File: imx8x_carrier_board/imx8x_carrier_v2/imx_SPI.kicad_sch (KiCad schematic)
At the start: 0 parts

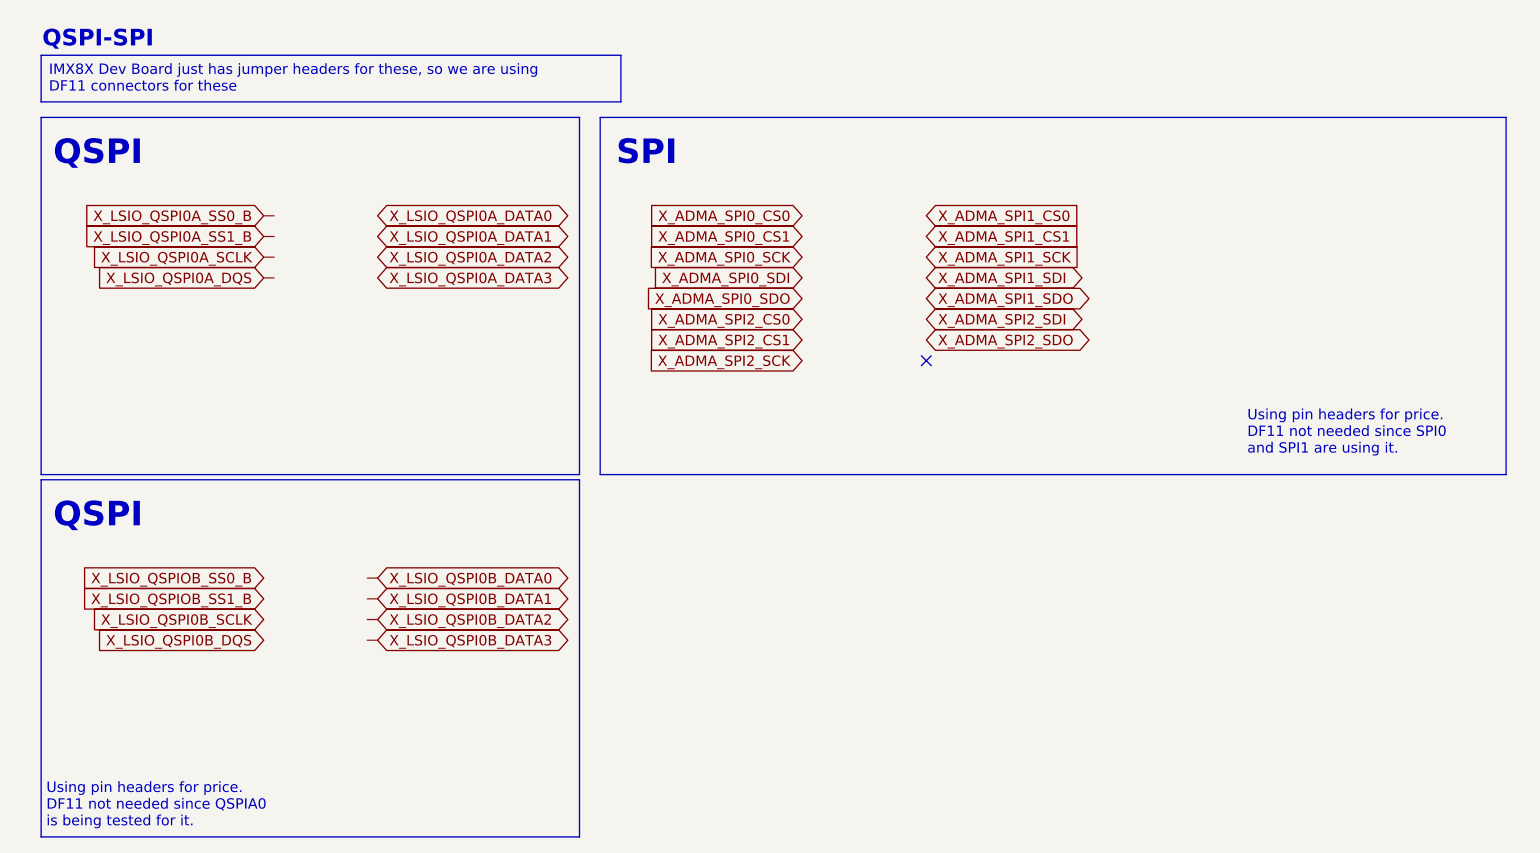
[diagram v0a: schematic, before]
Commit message: Layout Changes
Consolidated the BOM a little bit, have to rerout
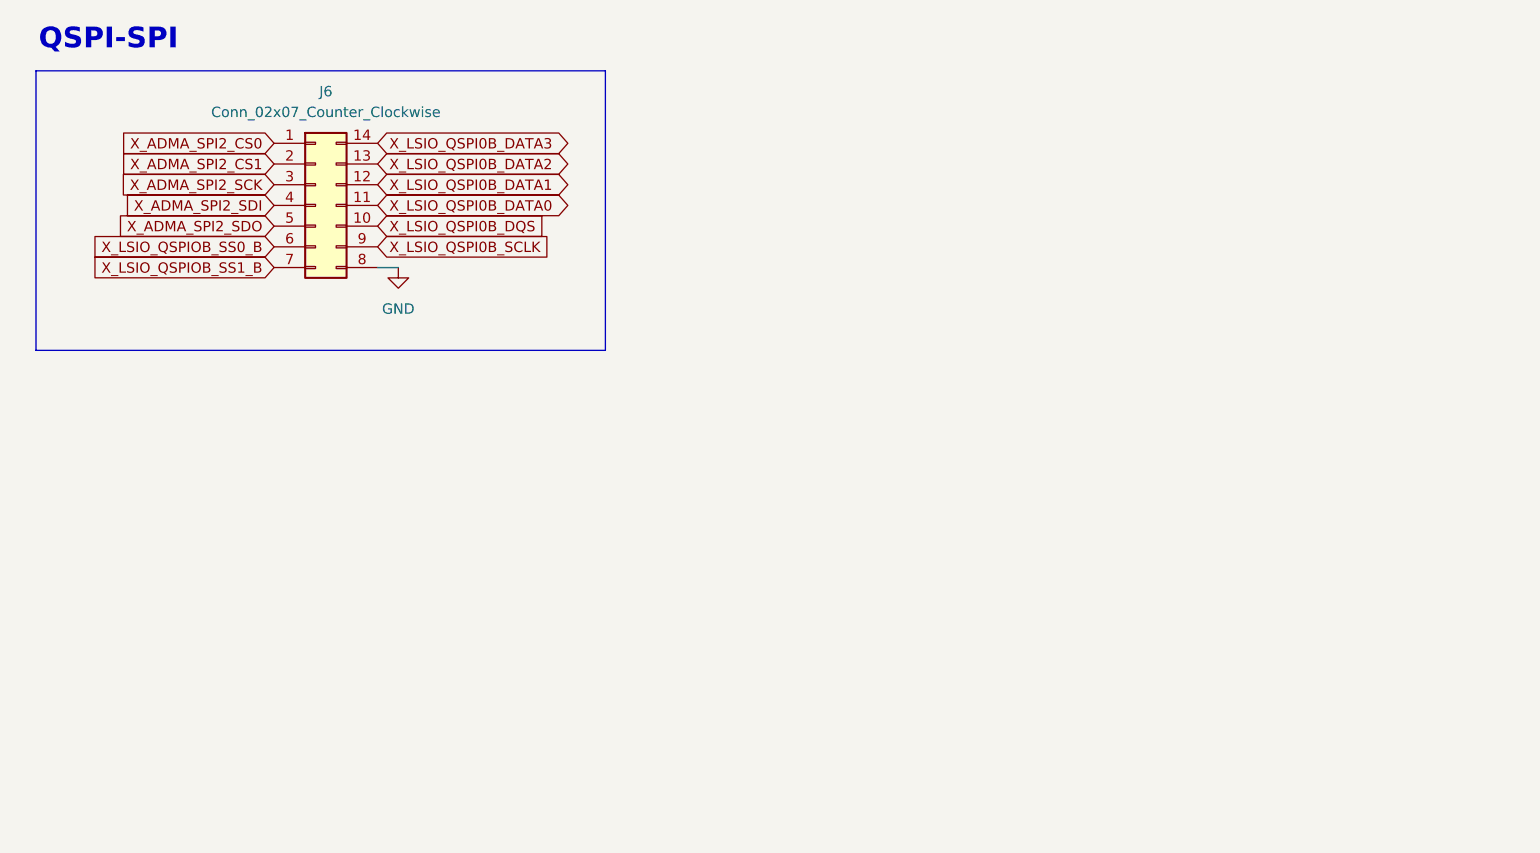
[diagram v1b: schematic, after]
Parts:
- added J6: Conn_02x07_Counter_Clockwise, Connector_PinHeader_2.54mm:PinHeader_2x07_P2.54mm_Vertical, symbol Connector_Generic:Conn_02x07_Counter_Clockwise
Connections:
- net X_ADMA_SPI2_CS0: now also J6.1 (Pin_1)
- net X_ADMA_SPI2_CS1: now also J6.2 (Pin_2)
- net X_ADMA_SPI2_SCK: now also J6.3 (Pin_3)
- net X_ADMA_SPI2_SDI: now also J6.4 (Pin_4)
- net X_ADMA_SPI2_SDO: now also J6.5 (Pin_5)
- net X_LSIO_QSPI0B_DATA0: now also J6.11 (Pin_11)
- net X_LSIO_QSPI0B_DATA1: now also J6.12 (Pin_12)
- net X_LSIO_QSPI0B_DATA2: now also J6.13 (Pin_13)
- net X_LSIO_QSPI0B_DATA3: now also J6.14 (Pin_14)
- net X_LSIO_QSPI0B_DQS: now also J6.10 (Pin_10)
- net X_LSIO_QSPI0B_SCLK: now also J6.9 (Pin_9)
- net X_LSIO_QSPIOB_SS0_B: now also J6.6 (Pin_6)
- net X_LSIO_QSPIOB_SS1_B: now also J6.7 (Pin_7)
- new net GND: J6.8 (Pin_8)
- no-connect marks 1 -> 0
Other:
- note removed: "QSPI"
- note removed: "SPI"
- note removed: "Using pin headers for price. DF11 not needed since QSPIA0 is being tested for it."
- note removed: "Using pin headers for price. DF11 not needed since SPI0 and SPI1 are using it."

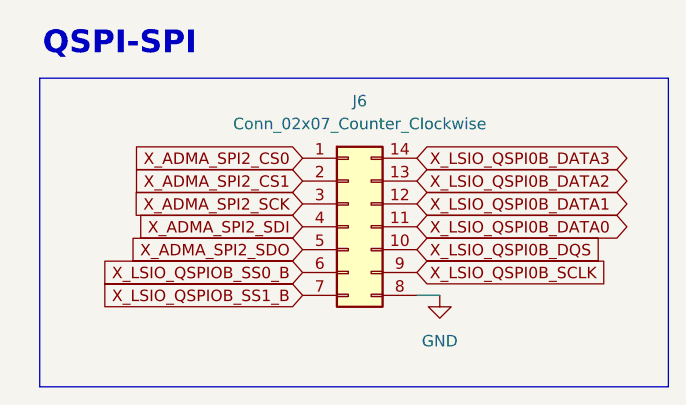
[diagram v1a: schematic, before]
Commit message: Finished Routing.
Completed routing and zone fills. Fixed some parts of the schematic as well.
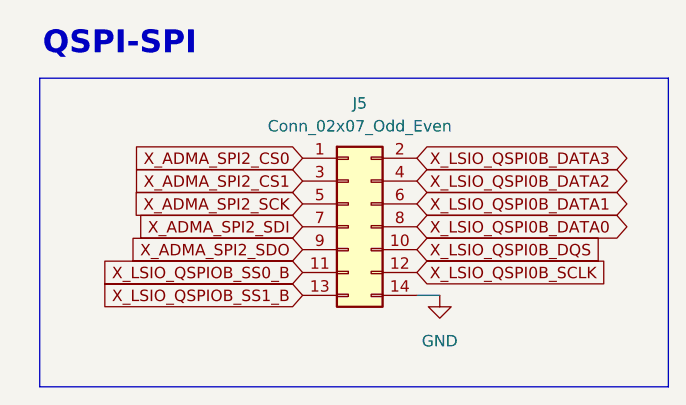
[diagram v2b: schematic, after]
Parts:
- removed J6: Conn_02x07_Counter_Clockwise, Connector_PinHeader_2.54mm:PinHeader_2x07_P2.54mm_Vertical, symbol Connector_Generic:Conn_02x07_Counter_Clockwise
- added J5: Conn_02x07_Odd_Even, imx8_carrier_board_footprints:PinHeader_2x07_P2.54mm_Vertical, symbol Connector_Generic:Conn_02x07_Odd_Even
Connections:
- net GND: now also J5.14 (Pin_14)
- net X_ADMA_SPI2_CS0: now also J5.1 (Pin_1)
- net X_ADMA_SPI2_CS1: now also J5.3 (Pin_3)
- net X_ADMA_SPI2_SCK: now also J5.5 (Pin_5)
- net X_ADMA_SPI2_SDI: now also J5.7 (Pin_7)
- net X_ADMA_SPI2_SDO: now also J5.9 (Pin_9)
- net X_LSIO_QSPI0B_DATA0: now also J5.8 (Pin_8)
- net X_LSIO_QSPI0B_DATA1: now also J5.6 (Pin_6)
- net X_LSIO_QSPI0B_DATA2: now also J5.4 (Pin_4)
- net X_LSIO_QSPI0B_DATA3: now also J5.2 (Pin_2)
- net X_LSIO_QSPI0B_DQS: now also J5.10 (Pin_10)
- net X_LSIO_QSPI0B_SCLK: now also J5.12 (Pin_12)
- net X_LSIO_QSPIOB_SS0_B: now also J5.11 (Pin_11)
- net X_LSIO_QSPIOB_SS1_B: now also J5.13 (Pin_13)
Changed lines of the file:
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@@
 	)
 	(symbol
-		(lib_id "Connector_Generic:Conn_02x07_Counter_Clockwise")
+		(lib_id "Connector_Generic:Conn_02x07_Odd_Even")
 		(at 48.26 36.83 0)
 		(unit 1)
@@
 		(on_board yes)
 		(dnp no)
-		(property "Reference" "J6"
-			(at 49.53 22.86 0)
+		(fields_autoplaced yes)
+		(property "Reference" "J5"
+			(at 49.53 23.114 0)
 			(effects
 				(font
@@
 			)
 		)
-		(property "Value" "Conn_02x07_Counter_Clockwise"
-			(at 49.53 25.4 0)
+		(property "Value" "Conn_02x07_Odd_Even"
+			(at 49.53 25.654 0)
 			(effects
 				(font
@@
 			)
 		)
-		(property "Footprint" "Connector_PinHeader_2.54mm:PinHeader_2x07_P2.54mm_Vertical"
+		(property "Footprint" "imx8_carrier_board_footprints:PinHeader_2x07_P2.54mm_Vertical"
 			(at 48.26 36.83 0)
 			(effects
@@
 			)
 		)
-		(property "Description" "Generic connector, double row, 02x07, counter clockwise pin numbering scheme (similar to DIP package numbering), script generated (kicad-library-utils/schlib/autogen/connector/)"
+		(property "Description" "Generic connector, double row, 02x07, odd/even pin numbering scheme (row 1 odd numbers, row 2 even numbers), script generated (kicad-library-utils/schlib/autogen/connector/)"
 			(at 48.26 36.83 0)
 			(effects
@@
 			)
 		)
-		(pin "3"
-		)
-		(pin "4"
-		)
-		(pin "2"
-		)
-		(pin "1"
-		)
 		(pin "10"
-		)
-		(pin "9"
-		)
-		(pin "13"
 		)
 		(pin "12"
@@
 		(pin "11"
 		)
+		(pin "6"
+		)
+		(pin "8"
+		)
+		(pin "3"
+		)
+		(pin "2"
+		)
 		(pin "5"
 		)
-		(pin "6"
+		(pin "13"
+		)
+		(pin "1"
+		)
+		(pin "4"
 		)
 		(pin "7"
 		)
-		(pin "8"
+		(pin "9"
 		)
 		(instances
 			(project "imx8x_carrier_v2"
 				(path "/4409cb5c-c5cc-45e5-ba22-666413441047/d29c5f61-1869-406e-b3b8-b642272ff287"
-					(reference "J6")
+					(reference "J5")
 					(unit 1)
 				)

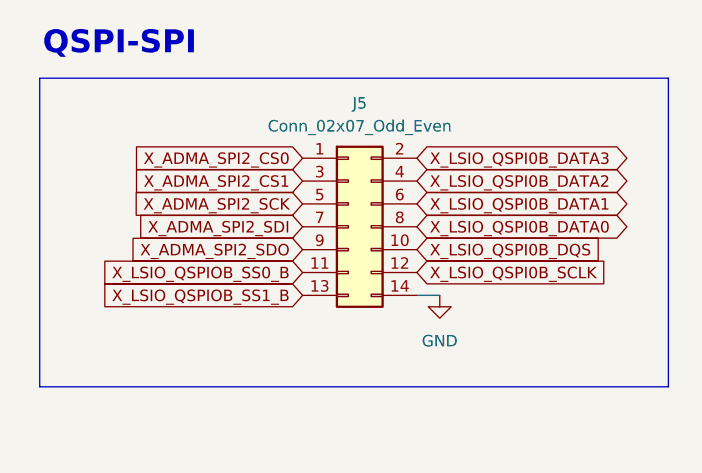
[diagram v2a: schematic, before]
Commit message: Changes some things
Made them all DF11. We have tons. And they can be secure.
Updated PinMux Sheet. 1 of everything, while also using whats preconfigured on the dev board for some stuff. Its good for final review before ordering. This should work.
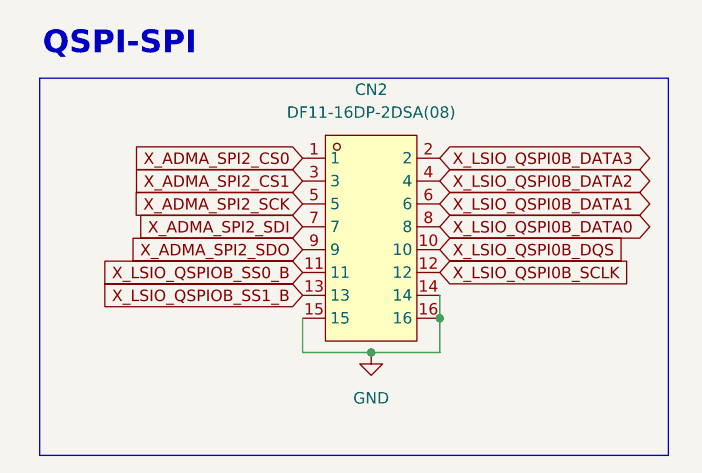
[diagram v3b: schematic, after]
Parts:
- removed J5: Conn_02x07_Odd_Even, imx8_carrier_board_footprints:PinHeader_2x07_P2.54mm_Vertical, symbol Connector_Generic:Conn_02x07_Odd_Even
- added CN2: DF11-16DP-2DSA(08), imx8_carrier_board_footprints:CONN-TH_DF11-16DP-2DSA-08, symbol imx8_carrier_board_symbol_library:DF11-16DP-2DSA(08)
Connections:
- net GND: now also CN2.14, CN2.15, CN2.16
- net X_ADMA_SPI2_CS0: now also CN2.1
- net X_ADMA_SPI2_CS1: now also CN2.3
- net X_ADMA_SPI2_SCK: now also CN2.5
- net X_ADMA_SPI2_SDI: now also CN2.7
- net X_ADMA_SPI2_SDO: now also CN2.9
- net X_LSIO_QSPI0B_DATA0: now also CN2.8
- net X_LSIO_QSPI0B_DATA1: now also CN2.6
- net X_LSIO_QSPI0B_DATA2: now also CN2.4
- net X_LSIO_QSPI0B_DATA3: now also CN2.2
- net X_LSIO_QSPI0B_DQS: now also CN2.10
- net X_LSIO_QSPI0B_SCLK: now also CN2.12
- net X_LSIO_QSPIOB_SS0_B: now also CN2.11
- net X_LSIO_QSPIOB_SS1_B: now also CN2.13
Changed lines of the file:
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@@
 	(rectangle
 		(start 13.97 20.32)
-		(end 83.82 54.61)
+		(end 83.82 62.23)
 		(stroke
 			(width 0)
@@
 		)
 	)
+	(junction
+		(at 58.42 46.99)
+		(diameter 0)
+		(color 0 0 0 0)
+	)
+	(junction
+		(at 50.8 50.8)
+		(diameter 0)
+		(color 0 0 0 0)
+	)
 	(wire
 		(pts
-			(xy 55.88 44.45) (xy 58.42 44.45)
+			(xy 58.42 46.99) (xy 58.42 50.8)
 		)
 		(stroke
@@
 		)
 	)
+	(wire
+		(pts
+			(xy 43.18 50.8) (xy 50.8 50.8)
+		)
+		(stroke
+			(width 0)
+			(type default)
+		)
+	)
+	(wire
+		(pts
+			(xy 58.42 44.45) (xy 58.42 46.99)
+		)
+		(stroke
+			(width 0)
+			(type default)
+		)
+	)
+	(wire
+		(pts
+			(xy 50.8 50.8) (xy 58.42 50.8)
+		)
+		(stroke
+			(width 0)
+			(type default)
+		)
+	)
+	(wire
+		(pts
+			(xy 43.18 46.99) (xy 43.18 50.8)
+		)
+		(stroke
+			(width 0)
+			(type default)
+		)
+	)
 	(global_label "X_ADMA_SPI2_CS0"
 		(shape input)
@@
 	(global_label "X_LSIO_QSPI0B_DATA1"
 		(shape bidirectional)
-		(at 55.88 34.29 0)
+		(at 58.42 34.29 0)
 		(fields_autoplaced yes)
 		(effects
@@
 		)
 		(property "Intersheetrefs" "${INTERSHEET_REFS}"
-			(at 80.7803 34.29 0)
+			(at 83.3203 34.29 0)
 			(effects
 				(font
@@
 	(global_label "X_LSIO_QSPI0B_DATA2"
 		(shape bidirectional)
-		(at 55.88 31.75 0)
+		(at 58.42 31.75 0)
 		(fields_autoplaced yes)
 		(effects
@@
 		)
 		(property "Intersheetrefs" "${INTERSHEET_REFS}"
-			(at 80.7803 31.75 0)
+			(at 83.3203 31.75 0)
 			(effects
 				(font
@@
 	(global_label "X_LSIO_QSPI0B_DATA0"
 		(shape bidirectional)
-		(at 55.88 36.83 0)
+		(at 58.42 36.83 0)
 		(fields_autoplaced yes)
 		(effects
@@
 		)
 		(property "Intersheetrefs" "${INTERSHEET_REFS}"
-			(at 80.7803 36.83 0)
+			(at 83.3203 36.83 0)
 			(effects
 				(font
@@
 	(global_label "X_LSIO_QSPI0B_DQS"
 		(shape input)
-		(at 55.88 39.37 0)
+		(at 58.42 39.37 0)
 		(fields_autoplaced yes)
 		(effects
@@
 		)
 		(property "Intersheetrefs" "${INTERSHEET_REFS}"
-			(at 77.8547 39.37 0)
+			(at 80.3947 39.37 0)
 			(effects
 				(font
@@
 	(global_label "X_LSIO_QSPI0B_DATA3"
 		(shape bidirectional)
-		(at 55.88 29.21 0)
+		(at 58.42 29.21 0)
 		(fields_autoplaced yes)
 		(effects
@@
 		)
 		(property "Intersheetrefs" "${INTERSHEET_REFS}"
-			(at 80.7803 29.21 0)
+			(at 83.3203 29.21 0)
 			(effects
 				(font
@@
 	(global_label "X_LSIO_QSPI0B_SCLK"
 		(shape input)
-		(at 55.88 41.91 0)
+		(at 58.42 41.91 0)
 		(fields_autoplaced yes)
 		(effects
@@
 		)
 		(property "Intersheetrefs" "${INTERSHEET_REFS}"
-			(at 78.8223 41.91 0)
+			(at 81.3623 41.91 0)
 			(effects
 				(font
@@
 	)
 	(symbol
-		(lib_id "Connector_Generic:Conn_02x07_Odd_Even")
-		(at 48.26 36.83 0)
+		(lib_id "imx8_carrier_board_symbol_library:DF11-16DP-2DSA(08)")
+		(at 50.8 38.1 0)
 		(unit 1)
 		(exclude_from_sim no)
@@
 		(dnp no)
 		(fields_autoplaced yes)
-		(property "Reference" "J5"
-			(at 49.53 23.114 0)
-			(effects
-				(font
-					(size 1.27 1.27)
-				)
-			)
-		)
-		(property "Value" "Conn_02x07_Odd_Even"
-			(at 49.53 25.654 0)
-			(effects
-				(font
-					(size 1.27 1.27)
-				)
-			)
-		)
-		(property "Footprint" "imx8_carrier_board_footprints:PinHeader_2x07_P2.54mm_Vertical"
-			(at 48.26 36.83 0)
-			(effects
-				(font
-					(size 1.27 1.27)
-				)
-				(hide yes)
-			)
-		)
-		(property "Datasheet" "~"
-			(at 48.26 36.83 0)
-			(effects
-				(font
-					(size 1.27 1.27)
-				)
-				(hide yes)
-			)
-		)
-		(property "Description" "Generic connector, double row, 02x07, odd/even pin numbering scheme (row 1 odd numbers, row 2 even numbers), script generated (kicad-library-utils/schlib/autogen/connector/)"
-			(at 48.26 36.83 0)
-			(effects
-				(font
-					(size 1.27 1.27)
-				)
-				(hide yes)
-			)
+		(property "Reference" "CN2"
+			(at 50.8 21.59 0)
+			(effects
+				(font
+					(size 1.27 1.27)
+				)
+			)
+		)
+		(property "Value" "DF11-16DP-2DSA(08)"
+			(at 50.8 24.13 0)
+			(effects
+				(font
+					(size 1.27 1.27)
+				)
+			)
+		)
+		(property "Footprint" "imx8_carrier_board_footprints:CONN-TH_DF11-16DP-2DSA-08"
+			(at 50.8 54.61 0)
+			(effects
+				(font
+					(size 1.27 1.27)
+				)
+				(hide yes)
+			)
+		)
+		(property "Datasheet" "https://lcsc.com/product-detail/Wire-To-Board-Wire-To-Wire-Connector_HRS-Hirose-HRS-DF11-16DP-2DSA-08_C530981.html"
+			(at 50.8 57.15 0)
+			(effects
+				(font
+					(size 1.27 1.27)
+				)
+				(hide yes)
+			)
+		)
+		(property "Description" "DF11 Connector"
+			(at 50.8 38.1 0)
+			(effects
+				(font
+					(size 1.27 1.27)
+				)
+				(hide yes)
+			)
+		)
+		(property "LCSC Part" "C530981"
+			(at 50.8 59.69 0)
+			(effects
+				(font
+					(size 1.27 1.27)
+				)
+				(hide yes)
+			)
+		)
+		(pin "1"
+		)
+		(pin "3"
+		)
+		(pin "11"
+		)
+		(pin "5"
+		)
+		(pin "15"
+		)
+		(pin "14"
+		)
+		(pin "13"
+		)
+		(pin "16"
+		)
+		(pin "7"
+		)
+		(pin "12"
+		)
+		(pin "6"
+		)
+		(pin "8"
 		)
 		(pin "10"
 		)
-		(pin "12"
-		)
-		(pin "14"
-		)
-		(pin "11"
-		)
-		(pin "6"
-		)
-		(pin "8"
-		)
-		(pin "3"
+		(pin "4"
+		)
+		(pin "9"
 		)
 		(pin "2"
 		)
-		(pin "5"
-		)
-		(pin "13"
-		)
-		(pin "1"
-		)
-		(pin "4"
-		)
-		(pin "7"
-		)
-		(pin "9"
-		)
 		(instances
-			(project "imx8x_carrier_v2"
+			(project ""
 				(path "/4409cb5c-c5cc-45e5-ba22-666413441047/d29c5f61-1869-406e-b3b8-b642272ff287"
-					(reference "J5")
+					(reference "CN2")
 					(unit 1)
 				)
@@
 	(symbol
 		(lib_id "power:GND")
-		(at 58.42 44.45 0)
+		(at 50.8 50.8 0)
 		(unit 1)
 		(exclude_from_sim no)
@@
 		(dnp no)
 		(fields_autoplaced yes)
-		(property "Reference" "#PWR09"
-			(at 58.42 50.8 0)
+		(property "Reference" "#PWR07"
+			(at 50.8 57.15 0)
 			(effects
 				(font
@@
 		)
 		(property "Value" "GND"
-			(at 58.42 49.53 0)
+			(at 50.8 55.88 0)
 			(effects
 				(font
@@
 		)
 		(property "Footprint" ""
-			(at 58.42 44.45 0)
+			(at 50.8 50.8 0)
 			(effects
 				(font
@@
 		)
 		(property "Datasheet" ""
-			(at 58.42 44.45 0)
+			(at 50.8 50.8 0)
 			(effects
 				(font
@@
 		)
 		(property "Description" "Power symbol creates a global label with name \"GND\" , ground"
-			(at 58.42 44.45 0)
+			(at 50.8 50.8 0)
 			(effects
 				(font
@@
 			(project ""
 				(path "/4409cb5c-c5cc-45e5-ba22-666413441047/d29c5f61-1869-406e-b3b8-b642272ff287"
-					(reference "#PWR09")
+					(reference "#PWR07")
 					(unit 1)
 				)
